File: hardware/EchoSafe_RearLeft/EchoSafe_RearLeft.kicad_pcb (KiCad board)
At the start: 2 copper layers, 46 x 40 mm, 4 parts, among them J1 Conn_Harness_07, M1 C0720B001F

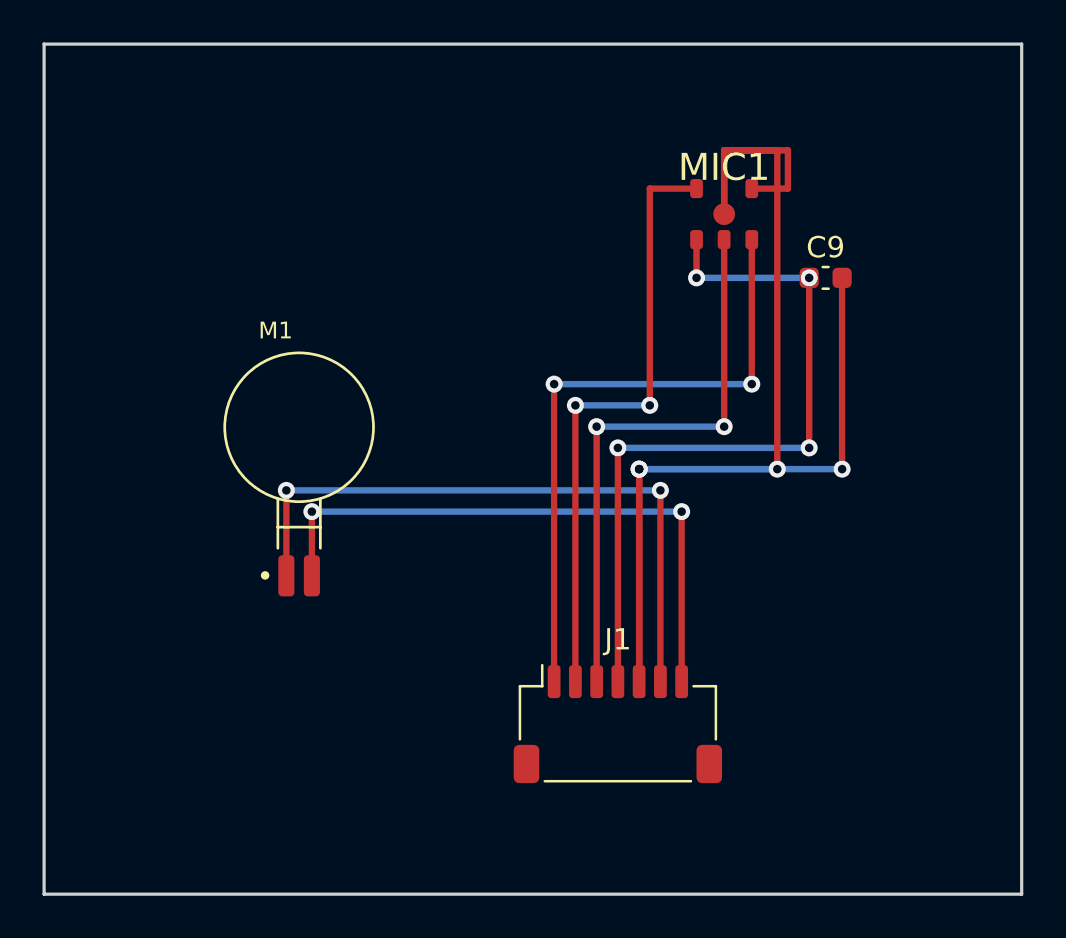
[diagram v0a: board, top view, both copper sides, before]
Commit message: Add acoustic port holes to mic modules, fix mic footprint pad positions
Adding the acoustic port hole (ICS-43434 datasheet: >=0.5mm diameter,
centered under the GND ring) exposed that the mic footprint's pad
positions -- authored earlier this session -- didn't match the real
chip at all: a simple 2x2-corner grid instead of the datasheet's actual
3-pad/2-pad row layout. Re-derived the correct pad positions from the
datasheet's mechanical package drawing (DS-000069 Rev 1.2, Figure 15)
via pixel-level measurement rather than reading dimension lines by eye,
cross-checked against reconstructed package width and the PIN#1
reference corner marker.

Also rebuilt the GND pad as a true annulus (was a solid disc) so the
hole has real clearance, shaved its OD from the datasheet's 1.625mm to
1.1mm to resolve a genuine overlap with the now-correctly-positioned
SCK/LR pads (real chip-scale pitch, not a mistake), and added a scoped
per-project DRC rule for the resulting sub-0.2mm chip-internal spacing
that the board's generic netclass rule doesn't accommodate.

Re-routed all 4 module boards from scratch after the pad reposition.
Verified via kicad-cli pcb drc: 0 violations, 0 unconnected pads on
every board. Still not a physical measurement -- flagged in CLAUDE.md
for verification against real hardware before fabrication.

Co-Authored-By: Claude Sonnet 5 <noreply@anthropic.com>
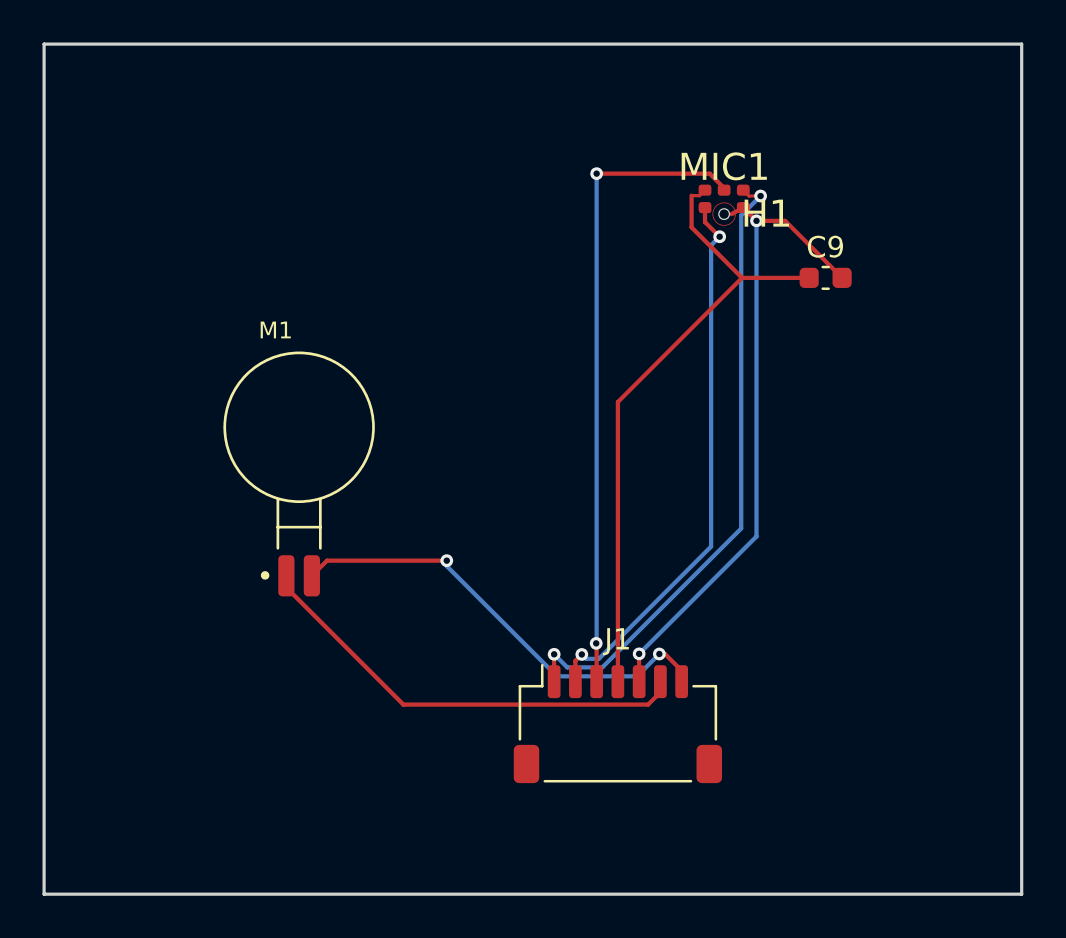
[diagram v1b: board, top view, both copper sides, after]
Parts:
- added H1: Acoustic_Port_0.5mm, Acoustic_Port_0.5mm, F.Cu at (32.0, 8.00)
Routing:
- net GND: track 75.0 -> 30.6 mm, vias 4 -> 2
- net MOTOR_BL_OUTP: track 30.6 -> 21.2 mm, vias 2 -> 0
- net MOTOR_BL_OUTN: track 28.4 -> 21.4 mm
- net 3V3_SYS: track 35.1 -> 30.2 mm, vias 4 -> 0
- net MIC_BOT_SD: track 26.8 -> 30.3 mm
- net MIC_BOT_SCK: track 28.9 -> 26.2 mm

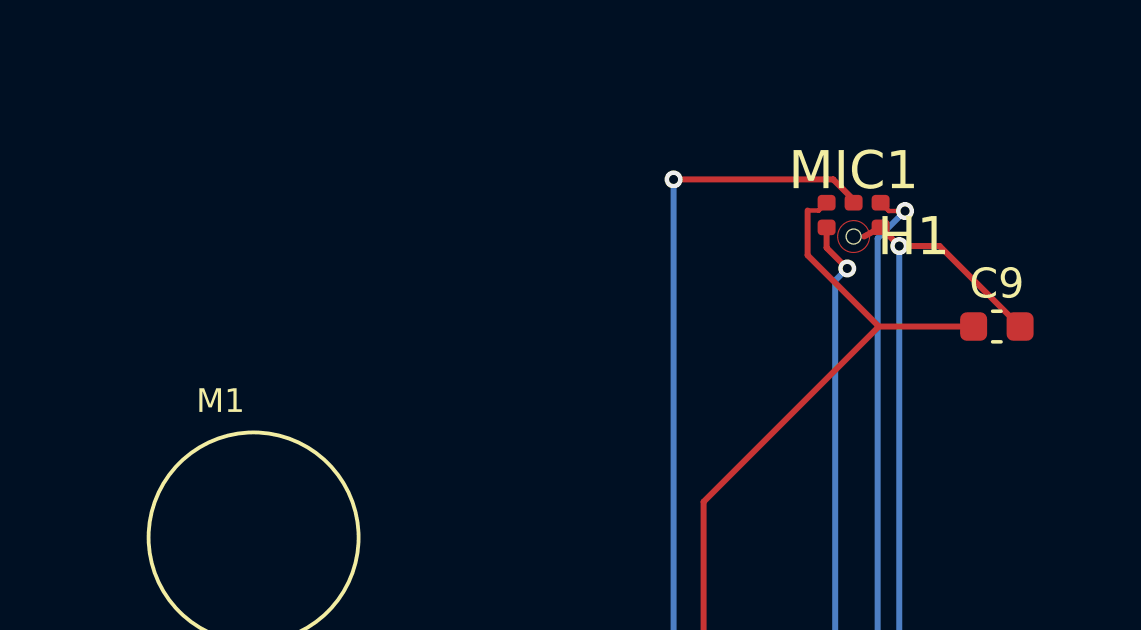
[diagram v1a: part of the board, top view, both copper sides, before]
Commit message: Visual/silkscreen review: fix footprint FPID prefixes and silkscreen overlaps
kicad-cli pcb drc was only ever run at default severity, which silently
excludes the silk_over_copper/silk_overlap/text_height checks. Re-running
with --severity-all, plus rendering true F.SilkS-only SVGs (previous
renders mixed in F.Fab assembly-doc text, making boards look far more
cluttered than they are), surfaced real issues:

- Every placed footprint on all 5 boards had lost its library prefix
  (bare name, no "Library:" qualifier) despite correct fp-lib-table
  registrations -- pcbnew's Python API doesn't preserve FPID library
  nicknames across a FootprintLoad()/board.Add() round-trip unless
  SetFPID() is called explicitly. Fixed across all 5 boards.
- The custom TP4056_Module footprint had its pads listing F.SilkS in
  their own layer set (guaranteed self-violation on every pad) and
  center-justified pin labels straddling the outline/pad edges. Fixed
  in the library footprint and re-synced onto the central pod.
- H1 (acoustic port) and M1 (motor) reference text overlapped MIC1's
  pads and undersized text vs. the board's minimum, respectively --
  fixed in their library footprints and re-synced onto all 4 modules.
- U2's reference sat on its own QFN thermal pad; C8's reference
  overlapped neighboring C4's silkscreen; U1/U2 each carried a literal
  duplicate coincident silkscreen text object (UltraLibrarian import
  artifact). All fixed.

All 5 boards now show 0 DRC violations at full severity (previously
only verified at default severity). Two items flagged but left
unfixed since they'd require hand-editing KiCad's own shared global
library footprints: J1/LS1 connectors have no pin-1 marker on the
physically-printed silkscreen (only on F.Fab), and U1's reference
will be hidden under the soldered ESP32 module.

Co-Authored-By: Claude Sonnet 5 <noreply@anthropic.com>
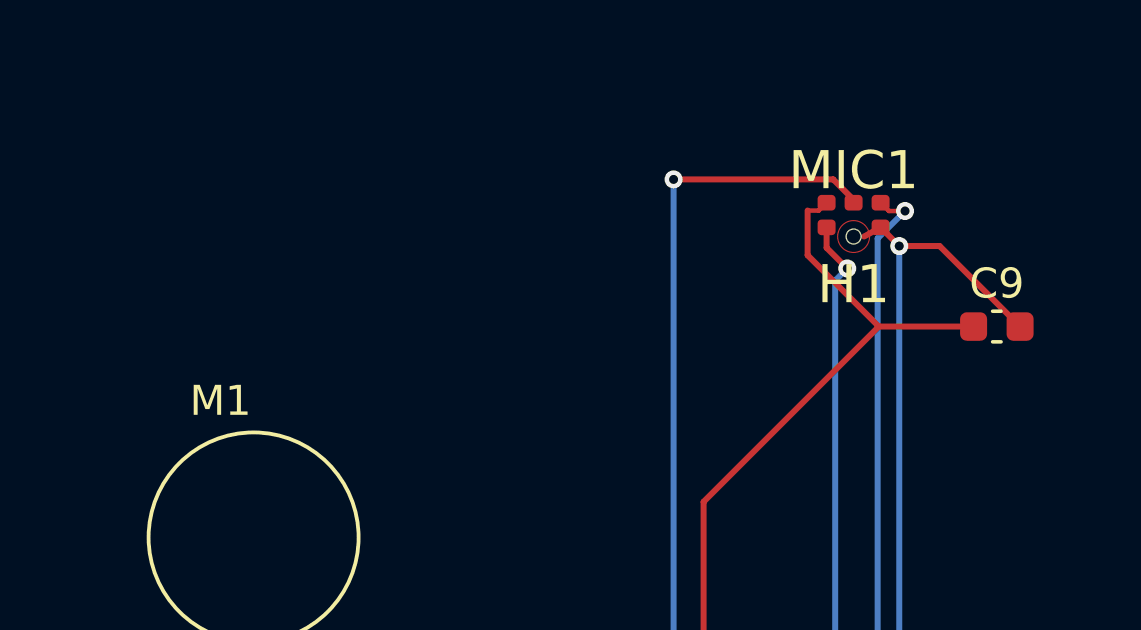
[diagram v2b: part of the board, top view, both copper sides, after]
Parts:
- C9: footprint C_0603_1608Metric -> Capacitor_SMD:C_0603_1608Metric
- H1: footprint Acoustic_Port_0.5mm -> ICS-43434:Acoustic_Port_0.5mm
- J1: footprint JST_SH_SM07B-SRSS-TB_1x07-1MP_P1.00mm_Horizontal -> Connector_JST:JST_SH_SM07B-SRSS-TB_1x07-1MP_P1.00mm_Horizontal
- M1: value C0720B001F -> XDCR_C0720B001F; footprint XDCR_C0720B001F -> C0720B001F:XDCR_C0720B001F
- MIC1: footprint ICS-43434_LGA6 -> ICS-43434:ICS-43434_LGA6

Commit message: Add pin-1 silkscreen markers and relocate U1's hidden reference
Follow-up to the visual/silkscreen review: both previously-flagged
items are now addressed.

- J1 (all 4 modules + central pod J2-J5) and LS1 (front modules) used
  KiCad's stock Connector_JST/Connector_Molex footprints, whose F.SilkS
  pin-1 indicator is only a subtle asymmetric notch in the outline
  (easy to miss at this scale) -- not, as first described, entirely
  absent. Rather than hand-edit KiCad's shared global libraries, added
  a project-local override library (lib/symbols/Connectors_PinMarked.pretty)
  with a bold pin-1 dot added to each of the 3 affected footprints, and
  resynced every affected instance onto it.
- U1 (ESP32-S3-WROOM-1)'s reference sat inside the module's own
  footprint outline (hidden once the module is soldered down).
  Checked every neighboring footprint and routed trace via pcbnew's
  Python API to see if it could move outside the outline into open
  board area -- it can't; this board was deliberately packed to a
  minimum practical 65x90mm and nothing borders U1 with room to spare.
  Moved the reference within the footprint's own interior instead, to
  a pocket clear of the trace and secondary pad cluster it previously
  sat on top of -- fully legible pre-assembly, same as before post-
  assembly (matches the original "cosmetic only" assessment).

All 5 boards re-verified at 0 DRC violations, full severity.

Co-Authored-By: Claude Sonnet 5 <noreply@anthropic.com>
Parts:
- J1: value Conn_Harness_07 -> JST_SH_SM07B-SRSS-TB_1x07-1MP_P1.00mm_Horizontal; footprint Connector_JST:JST_SH_SM07B-SRSS-TB_1x07-1MP_P1.00mm_Horizontal -> Connectors_PinMarked:JST_SH_SM07B-SRSS-TB_1x07-1MP_P1.00mm_Horizontal
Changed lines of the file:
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@@
 		)
 	)
-	(footprint "Connector_JST:JST_SH_SM07B-SRSS-TB_1x07-1MP_P1.00mm_Horizontal"
+	(footprint "Connectors_PinMarked:JST_SH_SM07B-SRSS-TB_1x07-1MP_P1.00mm_Horizontal"
 		(layer "F.Cu")
 		(at 27 32)
-		(descr "JST SH series connector, SM07B-SRSS-TB (http://www.jst-mfg.com/product/pdf/eng/eSH.pdf), generated with kicad-footprint-generator")
+		(descr "JST SH series connector, SM07B-SRSS-TB (http://www.jst-mfg.com/product/pdf/eng/eSH.pdf), generated with kicad-footprint-generator. Local project override of KiCad's stock Connector_JST footprint: adds a bold pin-1 dot on F.SilkS (the stock footprint only marks pin 1 with a subtle asymmetric notch in the outline, easy to miss at this scale) -- see CLAUDE.md Visual/Silkscreen Review.")
 		(tags "connector JST SH horizontal")
 		(property "Reference" "J1"
@@
 			)
 		)
-		(property "Value" "Conn_Harness_07"
+		(property "Value" "JST_SH_SM07B-SRSS-TB_1x07-1MP_P1.00mm_Horizontal"
 			(at 0 3.98 0)
 			(layer "F.Fab")
@@
 			(layer "F.SilkS")
 		)
+		(fp_circle
+			(center -3.9 -2)
+			(end -3.7 -2)
+			(stroke
+				(width 0.1)
+				(type solid)
+			)
+			(fill solid)
+			(layer "F.SilkS")
+		)
